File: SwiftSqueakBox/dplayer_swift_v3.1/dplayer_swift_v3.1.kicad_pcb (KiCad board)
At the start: 2 copper layers, 63.7 x 40.8 mm, 15 parts, among them SW1 Reset, U1 ATtiny85-20P, U2 dfplayer

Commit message: update pcb and schematic
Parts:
- added J2: ADKEY, Connector_PinHeader_2.00mm:PinHeader_1x03_P2.00mm_Vertical, F.Cu at (159.1, 84.0)
- added J3: DAC, Connector_PinHeader_2.00mm:PinHeader_1x03_P2.00mm_Vertical, F.Cu at (137.1, 102.3)
- Power: footprint Connector_PinHeader_2.54mm:PinHeader_2x01_P2.54mm_Vertical -> Connector_PinHeader_2.00mm:PinHeader_1x02_P2.00mm_Vertical
- U1: value ATtiny85-20P -> ATtiny85/45
- moved Power 7.89 mm to (147.3, 83.8), turned to 90 degrees
- moved LS1 2.93 mm to (137.1, 106.7)
- moved U2 1.04 mm to (151.1, 91.1)
- renumbered R3 to R1, R1 to R2, R2 to R3, SW1 to SW2
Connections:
- Power pad 1: +5V -> GND
- Power pad 2: GND -> +5V
- U2 pad 10: (no net) -> GND
- U2 pad 12: (no net) -> Net-(U2-Pad12)
- U2 pad 13: (no net) -> Net-(U2-Pad13)
- U2 pad 4: (no net) -> Net-(U2-Pad4)
- U2 pad 5: (no net) -> Net-(U2-Pad5)
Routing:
- net Net-(U2-Pad12): track 0.00 -> 20.0 mm
- net Net-(U2-Pad13): track 0.00 -> 16.6 mm
- net GND: track 99.5 -> 109.5 mm
- net +5V: track 94.1 -> 84.7 mm
- net Net-(U2-Pad4): track 0.00 -> 6.89 mm
- net Net-(U2-Pad5): track 0.00 -> 6.82 mm
- net Net-(LS1-Pad2): track 8.74 -> 6.49 mm
- net Net-(U1-Pad2): track 76.4 -> 78.3 mm
- net Net-(U1-Pad5): track 17.6 -> 16.6 mm
- net Net-(R3-Pad1): track 5.83 -> 4.79 mm
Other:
- board text added: "2"
- board text added: "K2_Gierzwaluw v.3.1"
- board text added: "L"
- board text added: "R"
- board text added: "SSB"
- board text added: "Volume"
- board text removed: "K2_Gierzwaluw v.3"

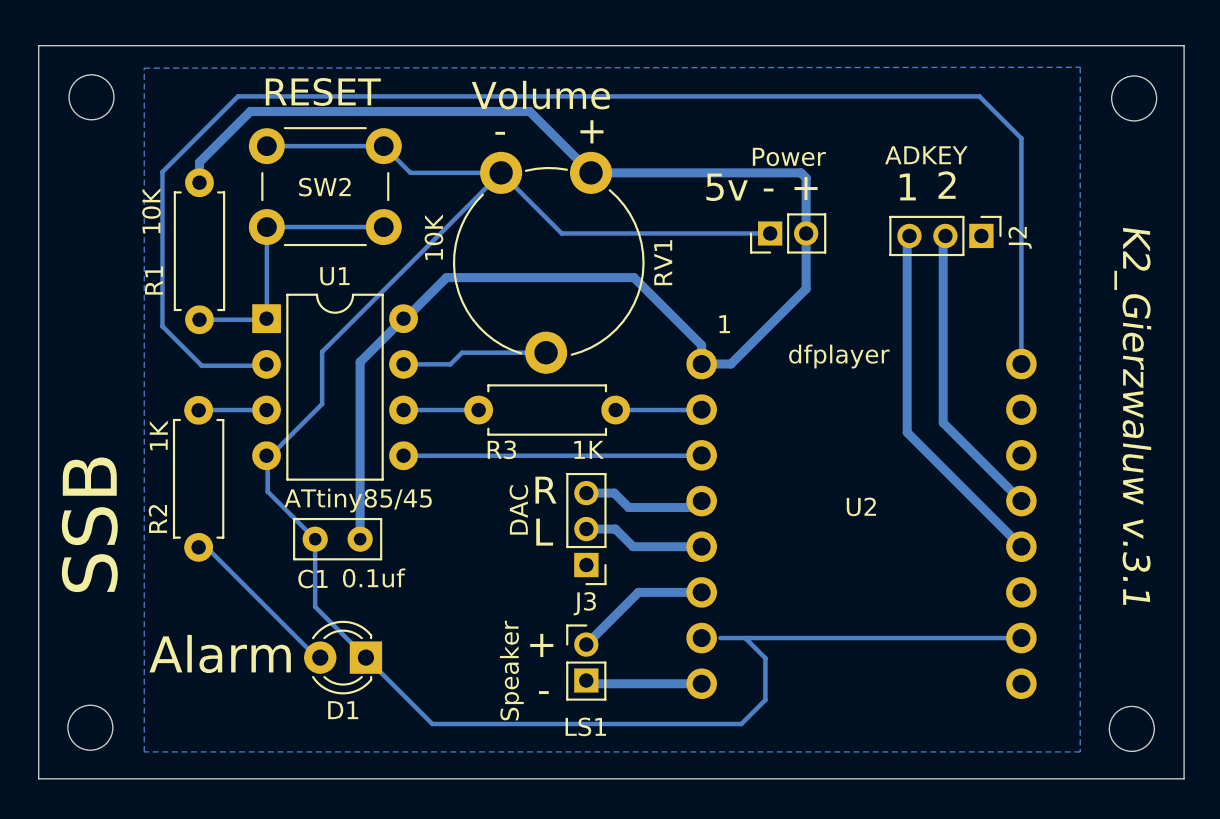
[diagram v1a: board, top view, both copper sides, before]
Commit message: Add amplifier, minor update to dplayer pcb
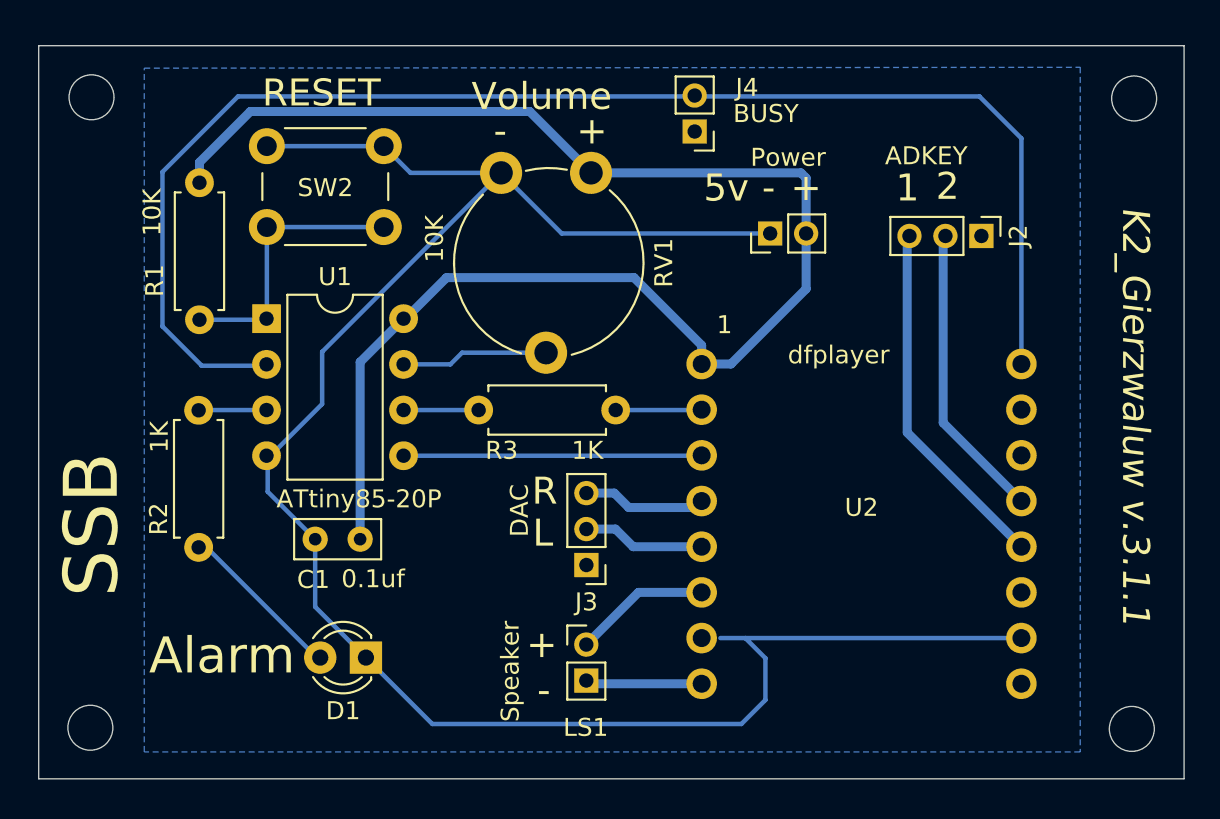
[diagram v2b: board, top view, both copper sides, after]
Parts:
- added J4: BUSY, Connector_PinHeader_2.00mm:PinHeader_1x02_P2.00mm_Vertical, F.Cu at (143.1, 78.2)
- U1: value ATtiny85/45 -> ATtiny85-20P
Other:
- board text added: "K2_Gierzwaluw v.3.1.1"
- board text removed: "K2_Gierzwaluw v.3.1"
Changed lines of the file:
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@@
   (net 6 "Net-(R2-Pad1)")
   (net 7 "Net-(U1-Pad2)")
-  (net 8 "Net-(U2-Pad5)")
+  (net 8 "Net-(J2-Pad2)")
   (net 9 "Net-(R3-Pad1)")
   (net 10 "Net-(R1-Pad2)")
@@
   (net 12 "Net-(RV1-Pad2)")
   (net 13 "Net-(U1-Pad5)")
-  (net 14 "Net-(U2-Pad13)")
-  (net 15 "Net-(U2-Pad12)")
-  (net 16 "Net-(U2-Pad4)")
+  (net 14 "Net-(J2-Pad3)")
+  (net 15 "Net-(J3-Pad2)")
+  (net 16 "Net-(J3-Pad3)")
   (footprint "Connector_PinHeader_2.00mm:PinHeader_1x02_P2.00mm_Vertical" (layer "F.Cu")
     (at 147.32 83.82 90)
@@
       (effects (font (size 1 1) (thickness 0.15)))
     )
-    (fp_text value "ATtiny85/45" (at 5.145837 10.028238) (layer "F.SilkS")
+    (fp_text value "ATtiny85-20P" (at 5.145837 10.028238) (layer "F.SilkS")
       (effects (font (size 1 1) (thickness 0.15)))
     )
@@
       (net 13 "Net-(U1-Pad5)") (pinfunction "TX") (pintype "input"))
     (pad "4" thru_hole circle locked (at -7.62 7.62) (size 1.7 1.7) (drill 1) (layers *.Cu *.Mask)
-      (net 16 "Net-(U2-Pad4)") (pinfunction "DAC_R") (pintype "output"))
+      (net 16 "Net-(J3-Pad3)") (pinfunction "DAC_R") (pintype "output"))
     (pad "5" thru_hole circle locked (at -7.62 10.16) (size 1.7 1.7) (drill 1) (layers *.Cu *.Mask)
-      (net 8 "Net-(U2-Pad5)") (pinfunction "DAC_L") (pintype "output"))
+      (net 15 "Net-(J3-Pad2)") (pinfunction "DAC_L") (pintype "output"))
     (pad "6" thru_hole circle locked (at -7.62 12.7) (size 1.7 1.7) (drill 1) (layers *.Cu *.Mask)
       (net 1 "Net-(LS1-Pad1)") (pinfunction "SPK1") (pintype "output"))
@@
     (pad "11" thru_hole circle locked (at 10.16 12.7) (size 1.7 1.7) (drill 1) (layers *.Cu *.Mask))
     (pad "12" thru_hole circle locked (at 10.16 10.16) (size 1.7 1.7) (drill 1) (layers *.Cu *.Mask)
-      (net 15 "Net-(U2-Pad12)") (pinfunction "ADKEY_1") (pintype "output"))
+      (net 14 "Net-(J2-Pad3)") (pinfunction "ADKEY_1") (pintype "output"))
     (pad "13" thru_hole circle locked (at 10.16 7.62) (size 1.7 1.7) (drill 1) (layers *.Cu *.Mask)
-      (net 14 "Net-(U2-Pad13)") (pinfunction "ADKEY_2") (pintype "output"))
+      (net 8 "Net-(J2-Pad2)") (pinfunction "ADKEY_2") (pintype "output"))
     (pad "14" thru_hole circle locked (at 10.16 5.08) (size 1.7 1.7) (drill 1) (layers *.Cu *.Mask))
     (pad "15" thru_hole circle locked (at 10.16 2.54) (size 1.7 1.7) (drill 1) (layers *.Cu *.Mask))
@@
       (net 4 "GND") (pinfunction "Pin_1") (pintype "passive"))
     (pad "2" thru_hole oval (at 0 2 180) (size 1.35 1.35) (drill 0.8) (layers *.Cu *.Mask)
-      (net 8 "Net-(U2-Pad5)") (pinfunction "Pin_2") (pintype "passive"))
+      (net 15 "Net-(J3-Pad2)") (pinfunction "Pin_2") (pintype "passive"))
     (pad "3" thru_hole oval (at 0 4 180) (size 1.35 1.35) (drill 0.8) (layers *.Cu *.Mask)
-      (net 16 "Net-(U2-Pad4)") (pinfunction "Pin_3") (pintype "passive"))
+      (net 16 "Net-(J3-Pad3)") (pinfunction "Pin_3") (pintype "passive"))
     (model "${KICAD6_3DMODEL_DIR}/Connector_PinHeader_2.00mm.3dshapes/PinHeader_1x03_P2.00mm_Vertical.wrl"
       (offset (xyz 0 0 0))
@@
       (net 4 "GND") (pinfunction "Pin_1") (pintype "passive"))
     (pad "2" thru_hole oval (at 0 2 270) (size 1.35 1.35) (drill 0.8) (layers *.Cu *.Mask)
-      (net 14 "Net-(U2-Pad13)") (pinfunction "Pin_2") (pintype "passive"))
+      (net 8 "Net-(J2-Pad2)") (pinfunction "Pin_2") (pintype "passive"))
     (pad "3" thru_hole oval (at 0 4 270) (size 1.35 1.35) (drill 0.8) (layers *.Cu *.Mask)
-      (net 15 "Net-(U2-Pad12)") (pinfunction "Pin_3") (pintype "passive"))
+      (net 14 "Net-(J2-Pad3)") (pinfunction "Pin_3") (pintype "passive"))
     (model "${KICAD6_3DMODEL_DIR}/Connector_PinHeader_2.00mm.3dshapes/PinHeader_1x03_P2.00mm_Vertical.wrl"
+      (offset (xyz 0 0 0))
+      (scale (xyz 1 1 1))
+      (rotate (xyz 0 0 0))
+    )
+  )
+  (footprint "Connector_PinHeader_2.00mm:PinHeader_1x02_P2.00mm_Vertical" (layer "F.Cu")
+    (at 143.123519 78.150806 180)
+    (descr "Through hole straight pin header, 1x02, 2.00mm pitch, single row")
+    (tags "Through hole pin header THT 1x02 2.00mm single row")
+    (property "Sheetfile" "dplayer_swift_v3.1.kicad_sch")
+    (property "Sheetname" "")
+    (attr through_hole)
+    (fp_text reference "J4" (at -2.911652 2.445787) (layer "F.SilkS")
+      (effects (font (size 1 1) (thickness 0.15)))
+    )
+    (fp_text value "BUSY" (at -3.959847 0.989961) (layer "F.SilkS")
+      (effects (font (size 1 1) (thickness 0.15)))
+    )
+    (fp_text user "${REFERENCE}" (at 0 1 90) (layer "F.Fab")
+      (effects (font (size 1 1) (thickness 0.15)))
+    )
+    (fp_line (start -1.06 0) (end -1.06 -1.06) (layer "F.SilkS") (width 0.12))
+    (fp_line (start -1.06 1) (end 1.06 1) (layer "F.SilkS") (width 0.12))
+    (fp_line (start 1.06 1) (end 1.06 3.06) (layer "F.SilkS") (width 0.12))
+    (fp_line (start -1.06 3.06) (end 1.06 3.06) (layer "F.SilkS") (width 0.12))
+    (fp_line (start -1.06 -1.06) (end 0 -1.06) (layer "F.SilkS") (width 0.12))
+    (fp_line (start -1.06 1) (end -1.06 3.06) (layer "F.SilkS") (width 0.12))
+    (fp_line (start -1.5 -1.5) (end -1.5 3.5) (layer "F.CrtYd") (width 0.05))
+    (fp_line (start -1.5 3.5) (end 1.5 3.5) (layer "F.CrtYd") (width 0.05))
+    (fp_line (start 1.5 -1.5) (end -1.5 -1.5) (layer "F.CrtYd") (width 0.05))
+    (fp_line (start 1.5 3.5) (end 1.5 -1.5) (layer "F.CrtYd") (width 0.05))
+    (fp_line (start 1 3) (end -1 3) (layer "F.Fab") (width 0.1))
+    (fp_line (start -1 3) (end -1 -0.5) (layer "F.Fab") (width 0.1))
+    (fp_line (start 1 -1) (end 1 3) (layer "F.Fab") (width 0.1))
+    (fp_line (start -1 -0.5) (end -0.5 -1) (layer "F.Fab") (width 0.1))
+    (fp_line (start -0.5 -1) (end 1 -1) (layer "F.Fab") (width 0.1))
+    (pad "1" thru_hole rect (at 0 0 180) (size 1.35 1.35) (drill 0.8) (layers *.Cu *.Mask)
+      (net 4 "GND") (pinfunction "Pin_1") (pintype "passive"))
+    (pad "2" thru_hole oval (at 0 2 180) (size 1.35 1.35) (drill 0.8) (layers *.Cu *.Mask)
+      (net 7 "Net-(U1-Pad2)") (pinfunction "Pin_2") (pintype "passive"))
+    (model "${KICAD6_3DMODEL_DIR}/Connector_PinHeader_2.00mm.3dshapes/PinHeader_1x02_P2.00mm_Vertical.wrl"
       (offset (xyz 0 0 0))
       (scale (xyz 1 1 1))
@@
     (effects (font (size 1.5 1.5) (thickness 0.3)) (justify mirror))
   )
-  (gr_text "K2_Gierzwaluw v.3.1" (at 167.64 93.98 -90) (layer "F.SilkS")
+  (gr_text "K2_Gierzwaluw v.3.1.1" (at 167.64 93.98 -90) (layer "F.SilkS")
     (effects (font (size 1.5 1.5) (thickness 0.3) italic))
   )
@@
   (segment (start 115.686522 91.174724) (end 119.343431 91.174724) (width 0.25) (layer "B.Cu") (net 7))
   (segment (start 113.527613 88.985971) (end 115.682764 91.141122) (width 0.25) (layer "B.Cu") (net 7))
-  (segment (start 143.51 101.238282) (end 139.7 101.238282) (width 0.5) (layer "B.Cu") (net 8))
-  (segment (start 139.7 101.238282) (end 138.718351 100.256633) (width 0.5) (layer "B.Cu") (net 8))
-  (segment (start 138.718351 100.256633) (end 137.100613 100.256633) (width 0.5) (layer "B.Cu") (net 8))
+  (segment (start 156.94 83.963313) (end 156.982081 83.921232) (width 0.2) (layer "F.Cu") (net 8))
+  (segment (start 161.29 98.698282) (end 156.94 94.348282) (width 0.5) (layer "B.Cu") (net 8))
+  (segment (start 156.94 94.348282) (end 156.94 83.963313) (width 0.5) (layer "B.Cu") (net 8))
   (segment (start 143.490103 93.638179) (end 143.51 93.618282) (width 0.25) (layer "B.Cu") (net 9))
   (segment (start 138.72979 93.638179) (end 143.490103 93.638179) (width 0.25) (layer "B.Cu") (net 9))
@@
   (segment (start 143.490103 96.178179) (end 143.51 96.158282) (width 0.25) (layer "B.Cu") (net 13))
   (segment (start 126.934163 96.178179) (end 143.490103 96.178179) (width 0.25) (layer "B.Cu") (net 13))
-  (segment (start 156.94 83.963313) (end 156.982081 83.921232) (width 0.2) (layer "F.Cu") (net 14))
-  (segment (start 161.29 98.698282) (end 156.94 94.348282) (width 0.5) (layer "B.Cu") (net 14))
-  (segment (start 156.94 94.348282) (end 156.94 83.963313) (width 0.5) (layer "B.Cu") (net 14))
-  (segment (start 154.94 83.963313) (end 154.982081 83.921232) (width 0.2) (layer "F.Cu") (net 15))
-  (segment (start 154.94 94.888282) (end 154.94 83.963313) (width 0.5) (layer "B.Cu") (net 15))
-  (segment (start 161.29 101.238282) (end 154.94 94.888282) (width 0.5) (layer "B.Cu") (net 15))
+  (segment (start 154.94 83.963313) (end 154.982081 83.921232) (width 0.2) (layer "F.Cu") (net 14))
+  (segment (start 154.94 94.888282) (end 154.94 83.963313) (width 0.5) (layer "B.Cu") (net 14))
+  (segment (start 161.29 101.238282) (end 154.94 94.888282) (width 0.5) (layer "B.Cu") (net 14))
+  (segment (start 143.51 101.238282) (end 139.7 101.238282) (width 0.5) (layer "B.Cu") (net 15))
+  (segment (start 139.7 101.238282) (end 138.718351 100.256633) (width 0.5) (layer "B.Cu") (net 15))
+  (segment (start 138.718351 100.256633) (end 137.100613 100.256633) (width 0.5) (layer "B.Cu") (net 15))
   (segment (start 143.51 98.698282) (end 143.148282 99.06) (width 0.2) (layer "F.Cu") (net 16))
   (segment (start 143.148282 99.06) (end 139.455802 99.06) (width 0.5) (layer "B.Cu") (net 16))

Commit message: Update SSB Schematic and pcb V3.1.2
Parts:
- removed ?: B, MountingHole:MountingHole_2.5mm
- removed ?: A, MountingHole:MountingHole_2.5mm
- removed ?: D, MountingHole:MountingHole_2.5mm
- removed ?: C, MountingHole:MountingHole_2.5mm
- removed LS1: Speaker, Connector_PinHeader_2.00mm:PinHeader_1x02_P2.00mm_Vertical
- removed Power: Power, Connector_PinHeader_2.00mm:PinHeader_1x02_P2.00mm_Vertical
- added J5: LS, Connector_JST:JST_PH_B2B-PH-K_1x02_P2.00mm_Vertical, F.Cu at (135.7, 108.2)
- added J6: Power, Connector_JST:JST_PH_B2B-PH-K_1x02_P2.00mm_Vertical, F.Cu at (149.3, 84.9)
- added J7: MUTE, Connector_JST:JST_PH_B2B-PH-K_1x02_P2.00mm_Vertical, F.Cu at (117.4, 106.2)
- added REF**: MountingHole_2.2mm_M2, MountingHole:MountingHole_2.2mm_M2, F.Cu at (109.2, 76.2)
- added REF**: MountingHole_2.2mm_M2, MountingHole:MountingHole_2.2mm_M2, F.Cu at (167.6, 111.8)
- added REF**: MountingHole_2.2mm_M2, MountingHole:MountingHole_2.2mm_M2, F.Cu at (167.6, 76.2)
- added REF**: MountingHole_2.2mm_M2, MountingHole:MountingHole_2.2mm_M2, F.Cu at (109.2, 111.8)
- J2, J3: footprint Connector_PinHeader_2.00mm:PinHeader_1x03_P2.00mm_Vertical -> Connector_JST:JST_PH_B3B-PH-K_1x03_P2.00mm_Vertical
- J4: footprint Connector_PinHeader_2.00mm:PinHeader_1x02_P2.00mm_Vertical -> Connector_JST:JST_PH_B2B-PH-K_1x02_P2.00mm_Vertical
- moved J4 15.8 mm to (158.9, 78.8)
- moved J3 3.72 mm to (135.7, 98.8), turned to -90 degrees
- moved J2 0.95 mm to (158.8, 84.9), turned to 180 degrees
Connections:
- J2 pad 1: GND -> Net-(J2-Pad1)
- J2 pad 3: Net-(J2-Pad3) -> GND
- J3 pad 1: GND -> Net-(J3-Pad1)
- J3 pad 3: Net-(J3-Pad3) -> GND
- J4 pad 1: GND -> Net-(J4-Pad1)
- J4 pad 2: Net-(U1-Pad2) -> GND
- U1 pad 2: Net-(U1-Pad2) -> Net-(J4-Pad1)
- U2 pad 12: Net-(J2-Pad3) -> Net-(J2-Pad2)
- U2 pad 13: Net-(J2-Pad2) -> Net-(J2-Pad1)
- U2 pad 16: Net-(U1-Pad2) -> Net-(J4-Pad1)
- U2 pad 4: Net-(J3-Pad3) -> Net-(J3-Pad1)
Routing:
- net Net-(J4-Pad1): track 0.00 -> 85.9 mm
- net Net-(U1-Pad2): track 78.3 -> 0.00 mm
- net GND: track 109.5 -> 166.5 mm
- net Net-(J2-Pad3): track 20.0 -> 0.00 mm
- net Net-(R2-Pad1): track 3.78 -> 20.1 mm
- net Net-(J2-Pad1): track 0.00 -> 14.8 mm
- net Net-(J3-Pad1): track 0.00 -> 9.97 mm
- net Net-(J3-Pad3): track 6.89 -> 0.00 mm
- net Net-(J5-Pad1): track 7.62 -> 9.74 mm
- net Net-(J5-Pad2): track 6.49 -> 8.40 mm
- net Net-(J2-Pad2): track 16.6 -> 18.2 mm
- net Net-(J3-Pad2): track 6.82 -> 8.02 mm
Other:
- board text added: "K2_Gierzwaluw v.3.1.2"
- board text added: "SSB___"
- board text added: "mSD-Card"
- board text removed: "K2_Gierzwaluw v.3.1.1"
- board text removed: "SSB"
